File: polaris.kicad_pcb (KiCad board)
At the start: 4 copper layers, 75 x 155 mm, 158 parts, among them J101 XT60-M, J102 SPI, J103 I2C, J104 PB, J105 SWD, J106 PYRO5, J107 PYRO4, J108 PYRO3, J109 PYRO2, J110 PYRO1, J111 PYRO0, J112 SERVO0, J113 SERVO1, J114 SERVO2, J115 SERVO3, J116 SERVO4, J117 SERVO5, J118 RADIO, J119 POWER, J301 USB_C_Receptacle_USB2.0_16P, J401 GNSS, J501 XT60-M, Q201 IRLZ44N, Q202 IRLZ44N, Q401 Q_NMOS, Q501 IRLZ44N, Q502 IRLZ44N, Q503 IRLZ44N, Q504 IRLZ44N, Q505 IRLZ44N, Q506 IRLZ44N, SW401 SW_Push, SW402 SW_Push, U1101 THD-2528-11SD-GF, U1201 W25Q128JVE, U201 BQ24005, U202 LM74700, U203 LM74700, U204 TLV75733PDBV, U205 LMR51430, U206 TPS7A2033PDBVR, U301 USBLC6-2SC6, U302 CH224K, U303 USBLC6-2SC6, U401 STM32F446VETx, U501 PC817, U502 PC817, U503 CD4051B, U504 PC817, U505 PC817, U506 PC817, U507 PC817, U601 ICM-42688-P, U701 LSM6DSO32TR, U801 MS5607, U901 LPS22HH, Y401 YXC YSX321SL

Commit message: Continued laying out traces
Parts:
- moved D404 50.1 mm to (146.0, 44.3)
- moved D402 50.1 mm to (146.0, 42.4)
- moved R405 50.1 mm to (141.6, 42.4)
- moved R408 50.1 mm to (141.6, 46.5)
- moved R409 50.1 mm to (141.6, 44.3)
- moved D401 50.1 mm to (146.0, 40.3)
- moved D403 50.1 mm to (146.0, 46.5)
- moved R404 50.1 mm to (141.6, 40.3)
- moved C414 0.67 mm to (124.6, 60.6)
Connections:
- U401 pad 85: /3_NavigationProcessor/NAV_STAT1 -> /3_NavigationProcessor/NAV_STAT4
- U401 pad 86: /3_NavigationProcessor/NAV_STAT2 -> /3_NavigationProcessor/NAV_STAT3
- U401 pad 87: /3_NavigationProcessor/NAV_STAT3 -> /3_NavigationProcessor/NAV_STAT2
- U401 pad 88: /3_NavigationProcessor/NAV_STAT4 -> /3_NavigationProcessor/NAV_STAT1
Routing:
- net /3_NavigationProcessor/RF_RX: track 0.00 -> 106.0 mm, vias 0 -> 3
- net /3_NavigationProcessor/RF_TX: track 0.00 -> 98.2 mm, vias 0 -> 1
- net /3_NavigationProcessor/SPI4_SCK: track 0.00 -> 82.2 mm, vias 0 -> 3
- net /3_NavigationProcessor/I2C2_SCL: track 0.00 -> 60.3 mm, vias 0 -> 2
- net /3_NavigationProcessor/SPI4_MOSI: track 0.00 -> 47.1 mm, vias 0 -> 1
- net /3_NavigationProcessor/SPI4_MISO: track 0.00 -> 44.4 mm, vias 0 -> 1
- net /3_NavigationProcessor/NAV_BUZZ: track 0.00 -> 44.1 mm, vias 0 -> 3
- net /3_NavigationProcessor/SPI4_NSS: track 0.00 -> 42.7 mm, vias 0 -> 1
- net /3_NavigationProcessor/I2C2_SDA: track 0.00 -> 26.5 mm, vias 0 -> 1
- net /3_NavigationProcessor/FLASH_IO0: track 0.00 -> 26.4 mm, vias 0 -> 1
- net /3_NavigationProcessor/NAV_STAT4: track 0.00 -> 12.0 mm, vias 0 -> 1
- net /3_NavigationProcessor/NAV_STAT3: track 0.00 -> 11.1 mm, vias 0 -> 1
- net /3_NavigationProcessor/SYS_SWCLK: track 30.8 -> 35.7 mm
- net /3_NavigationProcessor/PB3: track 33.7 -> 37.8 mm
- net /3_NavigationProcessor/PB4: track 33.7 -> 37.7 mm
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
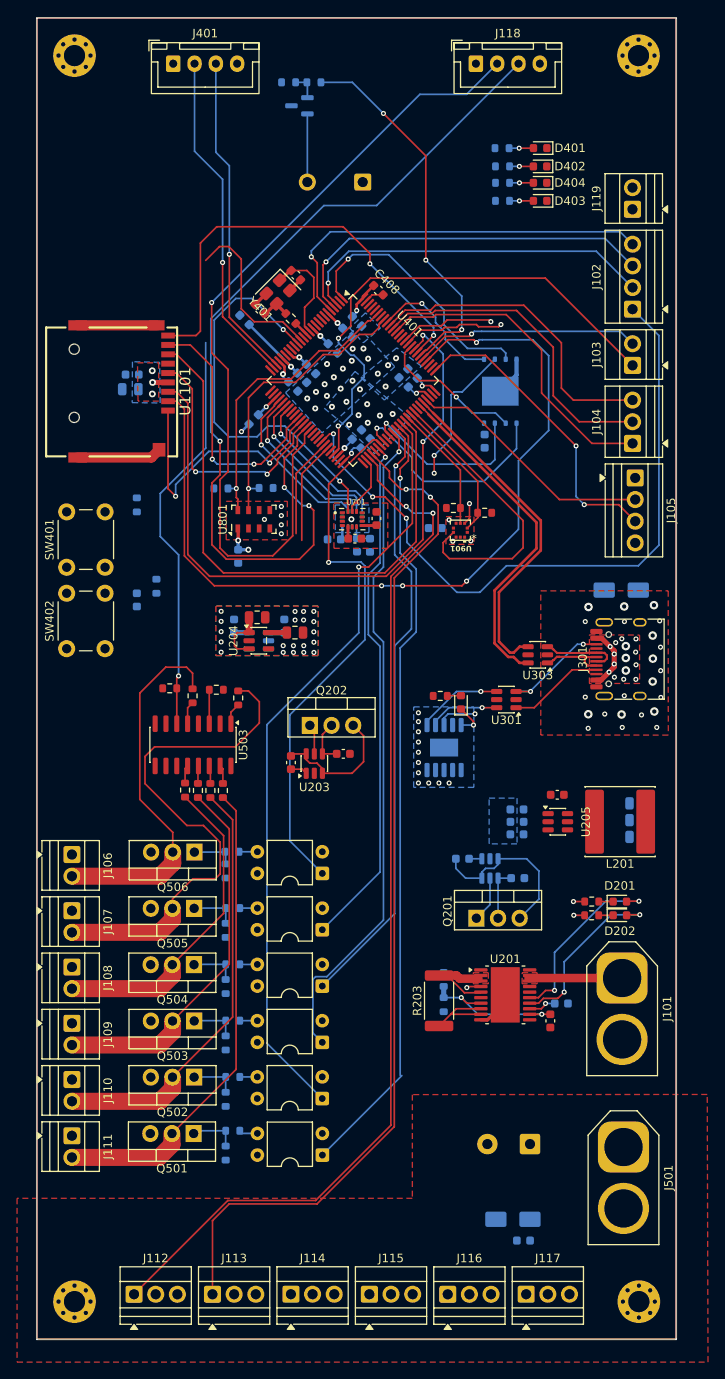
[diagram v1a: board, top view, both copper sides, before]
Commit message: Continued laying traces
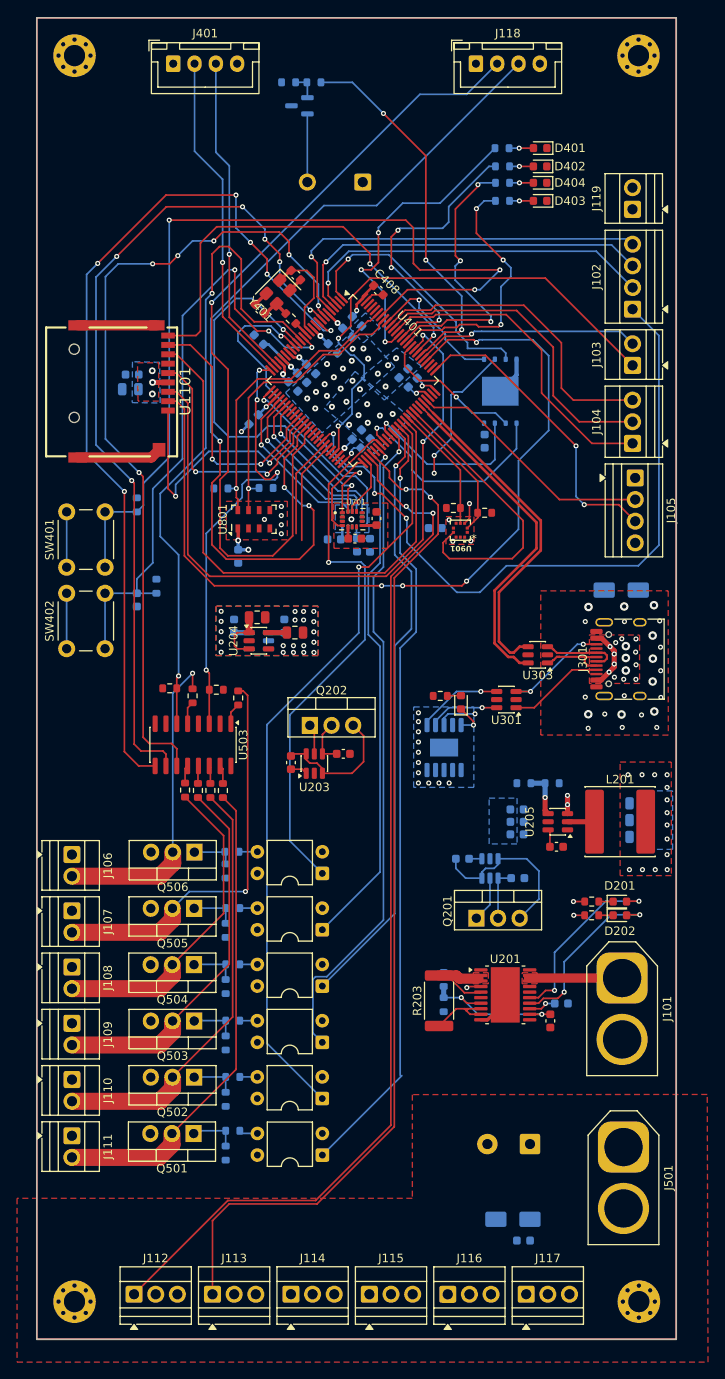
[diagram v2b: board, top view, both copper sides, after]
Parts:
- moved R207 8.50 mm to (144.1, 114.8), turned to 180 degrees
- moved R206 8.04 mm to (147.4, 114.8), turned to 180 degrees
- moved C212 6.10 mm to (148.0, 122.2), turned to 0 degrees
- moved C403 2.86 mm to (113.0, 62.7)
- turned C207 to 180 degrees
- turned C209 to 180 degrees
- turned C210 to 180 degrees
- turned C214 to 180 degrees
- turned C215 to 180 degrees
- turned C217 to 180 degrees
- turned L201 to 0 degrees
- turned U205 to 180 degrees
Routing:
- net /3_NavigationProcessor/MUX_C: track 0.00 -> 106.4 mm, vias 0 -> 6
- net Net-(U401-BOOT0): track 0.00 -> 105.9 mm, vias 0 -> 3
- net /3_NavigationProcessor/MUX_B: track 0.00 -> 100.0 mm, vias 0 -> 6
- net /3_NavigationProcessor/MUX_A: track 0.00 -> 97.0 mm, vias 0 -> 6
- net Net-(U401-NRST): track 0.00 -> 72.7 mm, vias 0 -> 3
- net /3_NavigationProcessor/PYRO_SENSE: track 3.99 -> 51.6 mm, vias 0 -> 4
- net /3_NavigationProcessor/LSM_MISO: track 0.00 -> 36.9 mm, vias 0 -> 2
- net /3_NavigationProcessor/NAV_STAT1: track 0.00 -> 35.6 mm, vias 0 -> 3
- net /3_NavigationProcessor/NAV_STAT2: track 0.00 -> 34.1 mm, vias 0 -> 3
- net /3_NavigationProcessor/ICM_INT: track 0.00 -> 22.7 mm, vias 0 -> 1
- net /3_NavigationProcessor/NAV_STAT3: track 11.1 -> 32.7 mm, vias 1 -> 3
- net /3_NavigationProcessor/NAV_STAT4: track 12.0 -> 30.4 mm, vias 1 -> 3
- net /4_Pyrochannels/PYRO_4: track 63.2 -> 50.0 mm, vias 0 -> 1
- net /3_NavigationProcessor/LSM_INT: track 0.00 -> 10.0 mm
- net /3_NavigationProcessor/~{MUX_EN}: track 67.7 -> 77.4 mm, vias 1 -> 2
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- added copper zone on B.Cu, net +5V
- added copper zone on F.Cu, net +5V
- removed copper zone on B.Cu, net POWER
